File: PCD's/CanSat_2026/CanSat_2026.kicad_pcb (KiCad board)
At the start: 2 copper layers, 66 x 66 mm, 9 parts, among them J1 Conn_01x02_Pin, J2 Conn_01x06, J3 Conn_01x06, J4 9DOF, J5 Conn_01x03_Pin, U1 LM1085-3.3, U2 LP5907MFX-1.8, U3 ESP32-WROOM-32D, U4 SN74AVC4T245PW

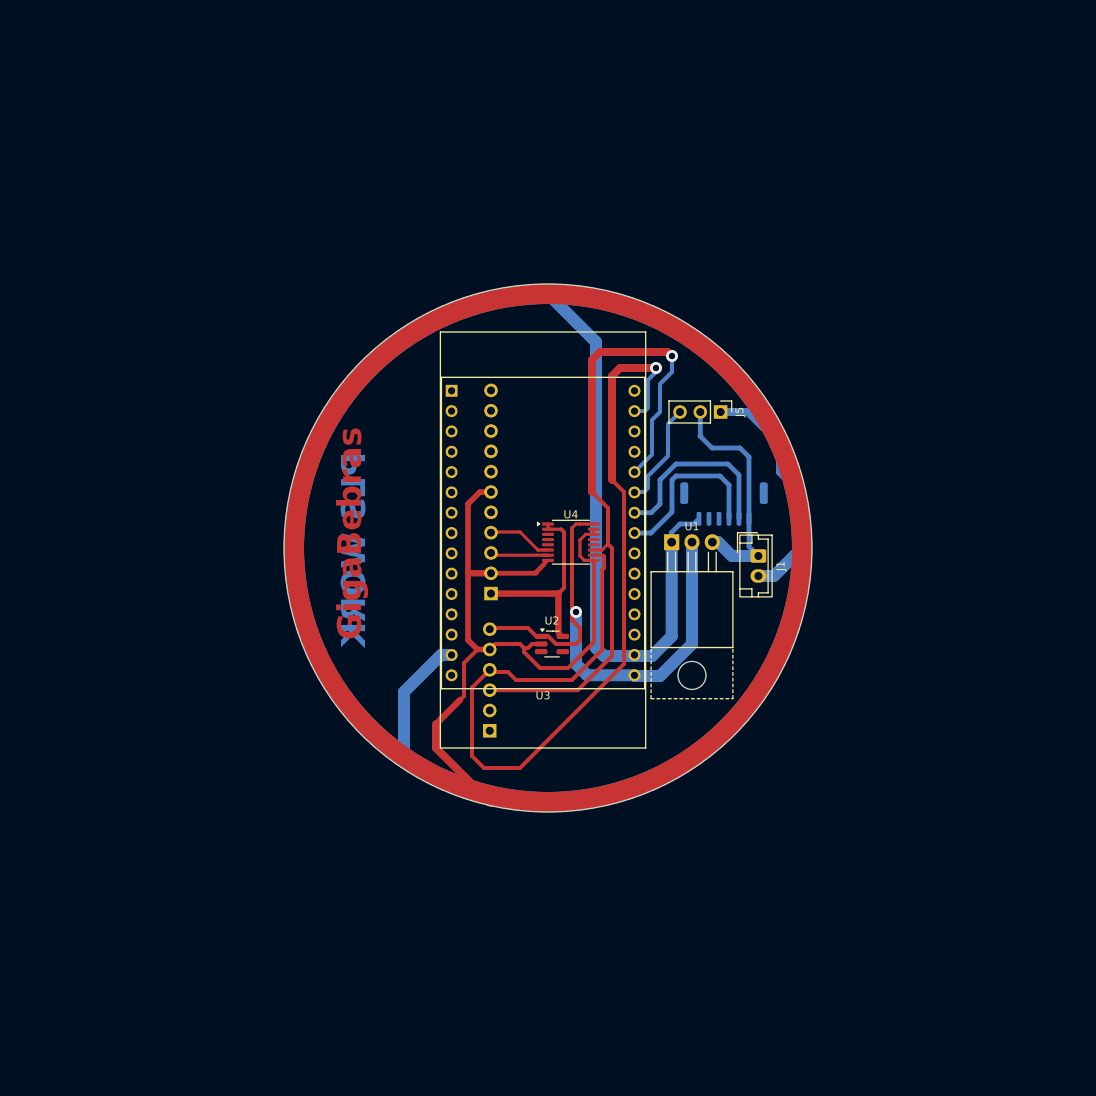
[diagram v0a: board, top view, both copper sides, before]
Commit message: Fix pcb for merge compatibility
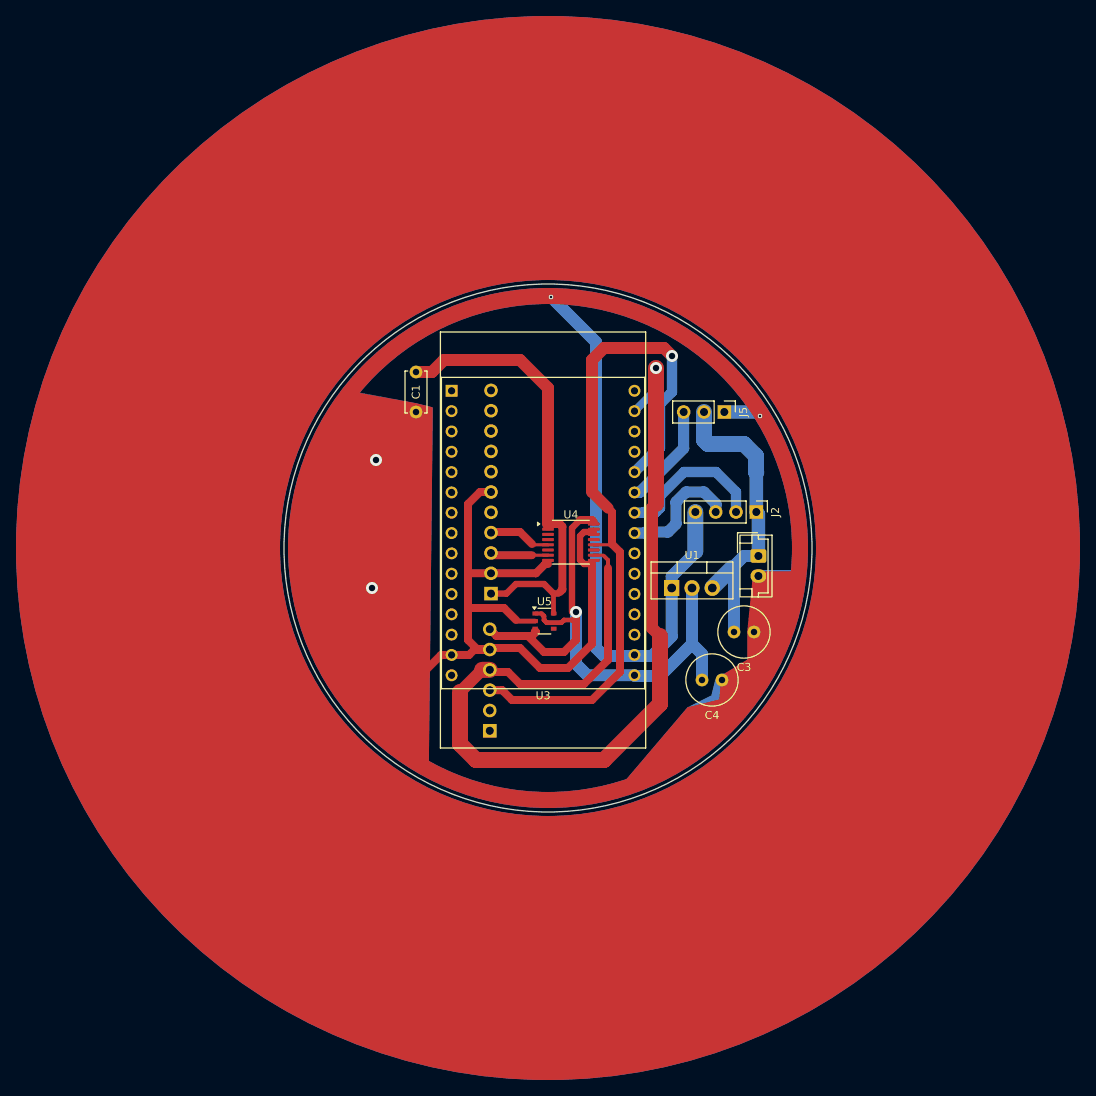
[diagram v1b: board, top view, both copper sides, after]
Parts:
- removed U2: LP5907MFX-1.8, Package_TO_SOT_SMD:SOT-23-5_HandSoldering
- added C1: 1uF_50V, Capacitor_THT:C_Disc_D5.0mm_W2.5mm_P5.00mm, F.Cu at (173.0, 48.0)
- added C3: 10uF_50V, Capacitor_THT:C_Radial_D6.3mm_H11.0mm_P2.50mm, F.Cu at (215.2, 80.5)
- added C4: 10uF_50V, Capacitor_THT:C_Radial_D6.3mm_H11.0mm_P2.50mm, F.Cu at (211.2, 86.5)
- added U5: NCP163ASN180T1G, Package_SO:TSOP-5_1.65x3.05mm_P0.95mm, F.Cu at (189.1, 79.1)
- J2: value Conn_01x06 -> Conn_01x04_Pin; footprint Connector_JST:JST_GH_SM06B-GHS-TB_1x06-1MP_P1.25mm_Horizontal -> Connector_PinHeader_2.54mm:PinHeader_1x04_P2.54mm_Vertical; moved to F.Cu
- J3: value Conn_01x06 -> BMP280
- J5: value Conn_01x03_Pin -> GPS
- U1: footprint Package_TO_SOT_THT:TO-220-3_Horizontal_TabUp -> Package_TO_SOT_THT:TO-220-3_Vertical
- moved U1 5.73 mm to (205.0, 75.0)
- moved J2 4.16 mm to (215.5, 65.5), turned to -90 degrees
- moved J5 0.46 mm to (211.5, 53.0)
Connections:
- J2 pad 1: GND -> +5V
- J2 pad 2: unconnected-(J2-Pin_2-Pad2) -> Net-(J2-Pin_2)
- J2 pad 3: unconnected-(J2-Pin_3-Pad3) -> Net-(J2-Pin_3)
- J2 pad 4: Net-(J2-Pin_4) -> GND
- U3 pad 29: Net-(J2-Pin_4) -> Net-(J2-Pin_3)
- U3 pad 30: Net-(J2-Pin_5) -> Net-(J2-Pin_2)
- U4 pad 11: Net-(J3-Pin_3) -> unconnected-(U4-2B1-Pad11)
- U4 pad 12: unconnected-(U4-1B2-Pad12) -> Net-(J3-Pin_3)
- U4 pad 5: unconnected-(U4-1A2-Pad5) -> Net-(J4-Pin_4)
- U4 pad 6: Net-(J4-Pin_4) -> unconnected-(U4-2A1-Pad6)
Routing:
- net +1V8: track 24.8 -> 58.5 mm
- net Net-(J2-Pin_5): track 23.4 -> 0.00 mm
- net Net-(J2-Pin_4): track 21.8 -> 0.00 mm
- net Net-(J2-Pin_2): track 0.00 -> 19.2 mm
- net Net-(J2-Pin_3): track 0.00 -> 15.5 mm
- net +5V: track 29.9 -> 39.0 mm
- net +3.3V: track 66.2 -> 73.5 mm
- net Net-(J3-Pin_3): track 84.3 -> 90.7 mm
- net GND: track 230.5 -> 225.7 mm, vias 0 -> 4
- net Net-(J3-Pin_4): track 116.1 -> 120.5 mm
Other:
- board text removed: "GigaBebras"
- board text removed: "PLS WORK"

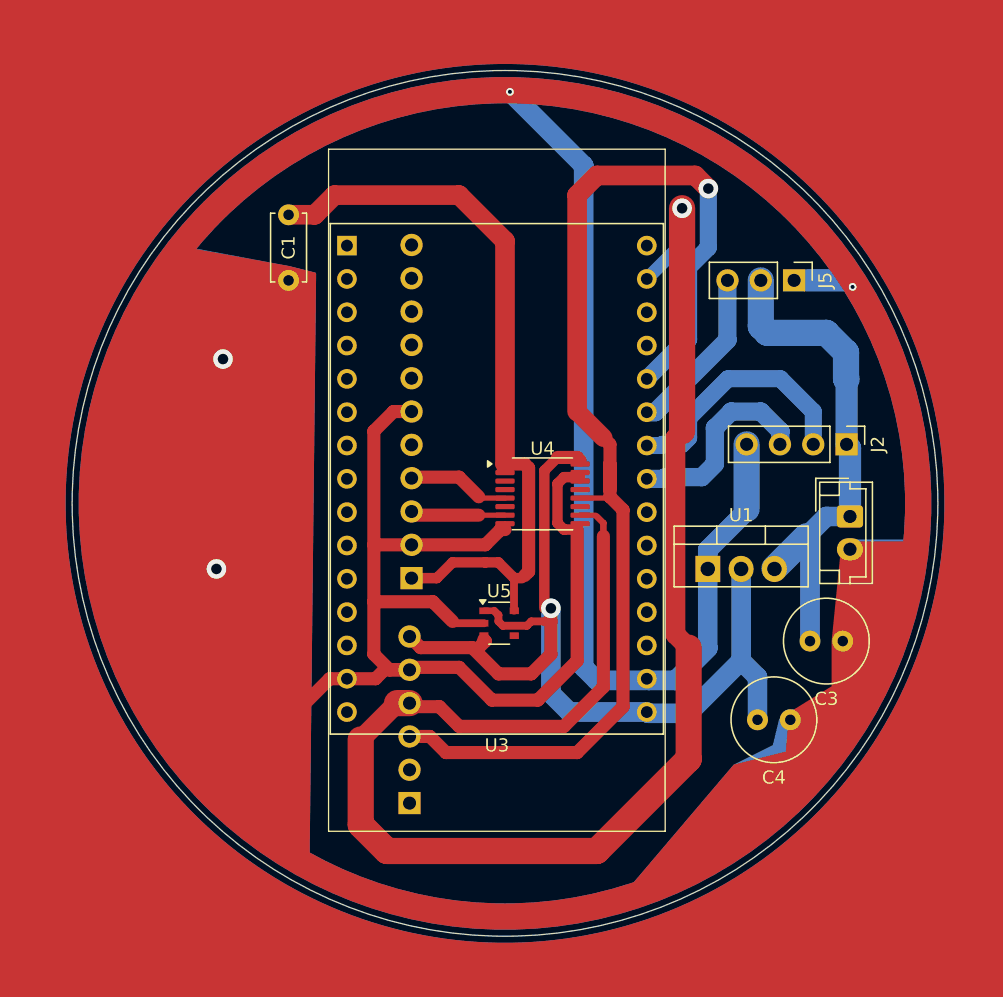
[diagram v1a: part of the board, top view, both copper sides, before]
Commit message: New PCB, progress on esp32 code
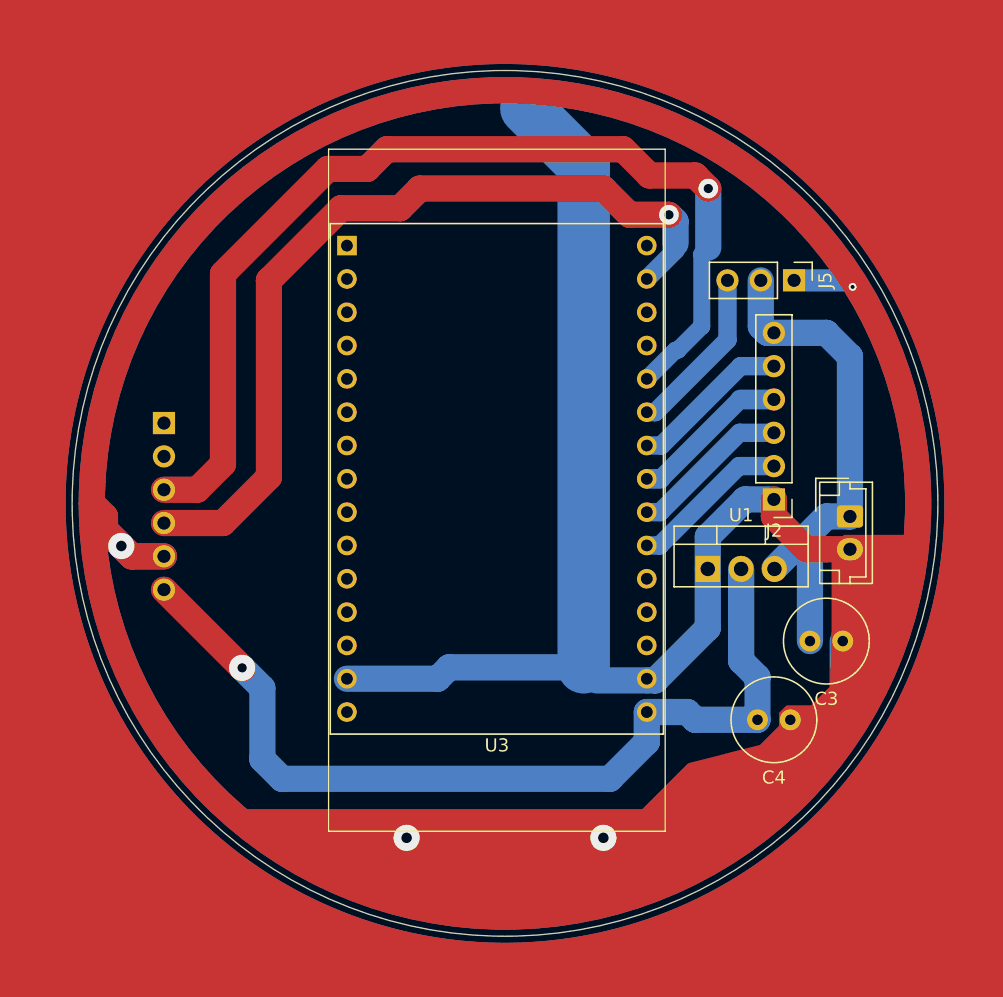
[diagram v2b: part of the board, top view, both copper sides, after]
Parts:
- removed C1: 1uF_50V, Capacitor_THT:C_Disc_D5.0mm_W2.5mm_P5.00mm
- removed J4: 9DOF, Connector_PinHeader_2.54mm:PinHeader_1x11_P2.54mm_Vertical
- removed U4: SN74AVC4T245PW, Package_SO:TSSOP-16_4.4x5mm_P0.65mm
- removed U5: NCP163ASN180T1G, Package_SO:TSOP-5_1.65x3.05mm_P0.95mm
- J2: value Conn_01x04_Pin -> Conn_01x06; footprint Connector_PinHeader_2.54mm:PinHeader_1x04_P2.54mm_Vertical -> Connector_PinHeader_2.54mm:PinHeader_1x06_P2.54mm_Vertical
- moved J3 34.5 mm to (163.5, 63.9), turned to 180 degrees
- moved J2 6.95 mm to (210.0, 69.7), turned to 180 degrees
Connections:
- J2 pad 1: +5V -> GND
- J2 pad 4: GND -> Net-(J2-Pin_4)
- U3 pad 27: unconnected-(U3-IO16-Pad27) -> Net-(J2-Pin_2)
- U3 pad 28: unconnected-(U3-IO17-Pad28) -> Net-(J2-Pin_3)
- U3 pad 29: Net-(J2-Pin_3) -> Net-(J2-Pin_4)
- U3 pad 30: Net-(J2-Pin_2) -> Net-(J2-Pin_5)
- U3 pad 31: Net-(J5-Pin_3) -> Net-(J4-Pin_5)
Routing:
- net GND: track 225.7 -> 142.6 mm
- net +1V8: track 58.5 -> 0.00 mm
- net Net-(J3-Pin_4): track 120.5 -> 64.7 mm
- net Net-(J2-Pin_4): track 0.00 -> 12.2 mm
- net Net-(J2-Pin_5): track 0.00 -> 12.2 mm
- net Net-(J3-Pin_3): track 90.7 -> 78.6 mm
- net Net-(J4-Pin_4): track 7.82 -> 0.00 mm
- net Net-(J4-Pin_3): track 7.24 -> 0.00 mm
- net Net-(J2-Pin_2): track 19.2 -> 12.2 mm
- net Net-(J2-Pin_3): track 15.5 -> 12.2 mm
- net +3.3V: track 73.5 -> 70.3 mm

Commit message: Progress on esp32
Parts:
- removed J2: Conn_01x06, Connector_PinHeader_2.54mm:PinHeader_1x06_P2.54mm_Vertical
- added J5: Conn_01x04_Pin, Connector_PinHeader_2.54mm:PinHeader_1x04_P2.54mm_Vertical, F.Cu at (206.5, 62.2)
- moved J1 8.38 mm to (213.3, 63.0)
- moved J3 5.02 mm to (164.5, 59.0)
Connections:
- U3 pad 27: Net-(J2-Pin_2) -> unconnected-(U3-IO16-Pad27)
- U3 pad 28: Net-(J2-Pin_3) -> unconnected-(U3-IO17-Pad28)
- U3 pad 29: Net-(J2-Pin_4) -> Net-(J5-Pin_3)
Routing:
- net GND: track 142.6 -> 158.2 mm, vias 4 -> 6
- net Net-(J2-Pin_4): track 12.2 -> 0.00 mm
- net Net-(J2-Pin_3): track 12.2 -> 0.00 mm
- net Net-(J2-Pin_2): track 12.2 -> 0.00 mm
- net Net-(J5-Pin_3): track 13.0 -> 19.7 mm
- net +5V: track 38.6 -> 45.1 mm
- net Net-(J3-Pin_4): track 64.7 -> 58.7 mm
- net Net-(J3-Pin_3): track 78.6 -> 72.7 mm
- net Net-(J5-Pin_2): track 12.2 -> 6.55 mm
- net +3.3V: track 70.3 -> 74.8 mm
